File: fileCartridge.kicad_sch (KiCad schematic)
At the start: 20 parts, among them U11 74AHCV17A, U12 74LVC3G17, U13 SN74LVC8T245, U14 SN74LVC8T245, U5 74LVC06A, U8 74LVC1G06, U9 SN74LVC8T245

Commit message: Fix some checker complaints
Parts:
- CART1: value (none) -> CARTRIDGE_C64; footprint (none) -> icomp:CARTRIDGE_C64_GERMAN
- X1: value (none) -> EXPANSION_PORT_C64_EDGE; footprint (none) -> RETRO_Innovations:MA100-22-2
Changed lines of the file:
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@@
     (comment 4 "Based on Orange Crab by Gregory Davill")
   )
+  (bus_alias "A_HIGH" (members "8" "9" "10" "11" "12" "13" "14" "15"))
   (junction (at 115.57 34.29) (diameter 0) (color 0 0 0 0)
   )
@@
     (stroke (width 0) (type default) (color 0 0 0 0))
   )
-  (wire (pts (xy 41.91 87.63) (xy 35.56 87.63))
+  (wire (pts (xy 41.91 87.63) (xy 39.37 87.63))
     (stroke (width 0) (type default) (color 0 0 0 0))
   )
@@
     (stroke (width 0) (type default) (color 0 0 0 0))
   )
-  (wire (pts (xy 24.13 91.44) (xy 19.05 91.44))
+  (wire (pts (xy 24.13 91.44) (xy 22.86 91.44))
     (stroke (width 0) (type default) (color 0 0 0 0))
   )
@@
     (effects (font (size 1.27 1.27)) (justify right bottom))
   )
-  (label "VCC" (at 203.2 92.71 180)
-    (effects (font (size 1.27 1.27)) (justify right bottom))
-  )
   (label "CINT6" (at 226.06 142.24 0)
     (effects (font (size 1.27 1.27)) (justify left bottom))
@@
     (effects (font (size 1.27 1.27)) (justify left bottom))
   )
-  (label "VCC" (at 35.56 87.63 0)
-    (effects (font (size 1.27 1.27)) (justify left bottom))
+  (label "{A_HIGH}" (at 171.45 92.71 180)
+    (effects (font (size 1.27 1.27)) (justify right bottom))
   )
   (label "10" (at 121.92 87.63 180)
@@
     (effects (font (size 1.27 1.27)) (justify left bottom))
   )
-  (label "VCC" (at 151.13 92.71 180)
-    (effects (font (size 1.27 1.27)) (justify right bottom))
-  )
   (label "15" (at 176.53 80.01 0)
     (effects (font (size 1.27 1.27)) (justify left bottom))
@@
   )
   (label "CD23" (at 74.93 74.93 0)
-    (effects (font (size 1.27 1.27)) (justify left bottom))
-  )
-  (label "VCC" (at 19.05 91.44 0)
     (effects (font (size 1.27 1.27)) (justify left bottom))
   )
@@
     )
   )
+  (global_label "P3.3V" (shape passive) (at 203.2 92.71 0) (fields_autoplaced)
+    (effects (font (size 1.27 1.27)) (justify left))
+    (property "Intersheet References" "${INTERSHEET_REFS}" (id 0) (at -62.23 -35.56 0)
+      (effects (font (size 1.27 1.27)) hide)
+    )
+  )
   (global_label "GAME" (shape input) (at 27.94 175.26 270) (fields_autoplaced)
     (effects (font (size 1.27 1.27)) (justify right))
@@
     )
   )
+  (global_label "P3.3V" (shape passive) (at 22.86 91.44 180) (fields_autoplaced)
+    (effects (font (size 1.27 1.27)) (justify right))
+    (property "Intersheet References" "${INTERSHEET_REFS}" (id 0) (at 288.29 219.71 0)
+      (effects (font (size 1.27 1.27)) hide)
+    )
+  )
   (global_label "EXROM" (shape input) (at 39.37 175.26 270) (fields_autoplaced)
     (effects (font (size 1.27 1.27)) (justify right))
@@
     )
   )
+  (global_label "P3.3V" (shape passive) (at 39.37 87.63 180) (fields_autoplaced)
+    (effects (font (size 1.27 1.27)) (justify right))
+    (property "Intersheet References" "${INTERSHEET_REFS}" (id 0) (at 304.8 215.9 0)
+      (effects (font (size 1.27 1.27)) hide)
+    )
+  )
   (global_label "A12" (shape bidirectional) (at 213.36 72.39 0) (fields_autoplaced)
     (effects (font (size 1.27 1.27)) (justify left))
@@
     )
   )
+  (global_label "P3.3V" (shape passive) (at 151.13 92.71 0) (fields_autoplaced)
+    (effects (font (size 1.27 1.27)) (justify left))
+    (property "Intersheet References" "${INTERSHEET_REFS}" (id 0) (at -114.3 -35.56 0)
+      (effects (font (size 1.27 1.27)) hide)
+    )
+  )
   (global_label "D_DIR" (shape input) (at 25.4 80.01 180) (fields_autoplaced)
     (effects (font (size 1.27 1.27)) (justify right))
@@
     )
   )
-  (symbol (lib_id "RETRO_Innovations:EXPANSION_PORT_C64_EDGE") (at 96.52 87.63 0) (mirror y) (unit 1)
+  (symbol (lib_name "EXPANSION_PORT_C64_EDGE_1") (lib_id "RETRO_Innovations:EXPANSION_PORT_C64_EDGE") (at 96.52 87.63 0) (mirror y) (unit 1)
     (in_bom no) (on_board yes)
     (property "Reference" "X1" (id 0) (at 96.52 52.578 0)
       (effects (font (size 1.4986 1.4986)))
     )
-    (property "Value" "" (id 1) (at 106.68 133.35 0)
+    (property "Value" "EXPANSION_PORT_C64_EDGE" (id 1) (at 86.36 133.35 0)
       (effects (font (size 1.4986 1.4986)) (justify left bottom) hide)
     )
-    (property "Footprint" "" (id 2) (at 96.52 87.63 0)
+    (property "Footprint" "RETRO_Innovations:MA100-22-2" (id 2) (at 96.52 87.63 0)
       (effects (font (size 1.27 1.27)) hide)
     )
@@
       (effects (font (size 1.4986 1.4986)) (justify left))
     )
-    (property "Value" "" (id 1) (at 241.3 113.03 0)
+    (property "Value" "EXPANSION_PORT_C64_EDGE" (id 1) (at 241.3 113.03 0)
       (effects (font (size 1.4986 1.4986)) (justify left bottom) hide)
     )
-    (property "Footprint" "" (id 2) (at 251.46 67.31 0)
+    (property "Footprint" "RETRO_Innovations:MA100-22-2" (id 2) (at 251.46 67.31 0)
       (effects (font (size 1.27 1.27)) hide)
     )
@@
       (effects (font (size 1.4986 1.4986)) (justify left))
     )
-    (property "Value" "" (id 1) (at 254 34.29 0)
-      (effects (font (size 1.27 1.27)) hide)
-    )
-    (property "Footprint" "" (id 2) (at 254 34.29 0)
-      (effects (font (size 1.27 1.27)) hide)
-    )
+    (property "Value" "CARTRIDGE_C64" (id 1) (at 254 34.29 0)
+      (effects (font (size 1.27 1.27)) hide)
+    )
+    (property "Footprint" "icomp:CARTRIDGE_C64_GERMAN" (id 2) (at 254 34.29 0)
+      (effects (font (size 1.27 1.27)) hide)
+    )

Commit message: Update Mouser prices
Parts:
- C4: Pricing (EUR) 0,04 -> 0,10
- U11: Pricing (EUR) 0,42 -> 0,44
- U12: Pricing (EUR) 0.47 -> 0.66
- U13, U14, U9: Pricing (EUR) 1,44 -> 1,56
- U5: Pricing (EUR) 0.35 -> 1,01
- U8: Pricing (EUR) 0.27 -> 0.34
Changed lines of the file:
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@@
       (effects (font (size 1.27 1.27)) hide)
     )
-    (property "Pricing (EUR)" "1,44" (id 5) (at 44.45 69.85 0)
+    (property "Pricing (EUR)" "1,56" (id 5) (at 44.45 69.85 0)
       (effects (font (size 1.27 1.27)) hide)
     )
@@
       (effects (font (size 1.27 1.27)) hide)
     )
-    (property "Pricing (EUR)" "1,44" (id 5) (at 194.31 74.93 0)
+    (property "Pricing (EUR)" "1,56" (id 5) (at 194.31 74.93 0)
       (effects (font (size 1.27 1.27)) hide)
     )
@@
       (effects (font (size 1.27 1.27)) hide)
     )
-    (property "Pricing (EUR)" "1,44" (id 5) (at 142.24 74.93 0)
+    (property "Pricing (EUR)" "1,56" (id 5) (at 142.24 74.93 0)
       (effects (font (size 1.27 1.27)) hide)
     )
@@
       (effects (font (size 1.27 1.27)) hide)
     )
-    (property "Pricing (EUR)" "0.27" (id 5) (at 49.53 152.4 0)
+    (property "Pricing (EUR)" "0.34" (id 5) (at 49.53 152.4 0)
       (effects (font (size 1.27 1.27)) hide)
     )
@@
       (effects (font (size 1.27 1.27)) hide)
     )
-    (property "Pricing (EUR)" "0,42" (id 5) (at 173.99 125.73 0)
+    (property "Pricing (EUR)" "0,44" (id 5) (at 173.99 125.73 0)
       (effects (font (size 1.27 1.27)) hide)
     )
@@
       (effects (font (size 1.27 1.27)) hide)
     )
-    (property "Pricing (EUR)" "0,42" (id 5) (at 114.3 143.51 0)
+    (property "Pricing (EUR)" "0,44" (id 5) (at 114.3 143.51 0)
       (effects (font (size 1.27 1.27)) hide)
     )
@@
       (effects (font (size 1.27 1.27)) hide)
     )
-    (property "Pricing (EUR)" "0,42" (id 5) (at 128.27 34.29 0)
+    (property "Pricing (EUR)" "0,44" (id 5) (at 128.27 34.29 0)
       (effects (font (size 1.27 1.27)) hide)
     )
@@
       (effects (font (size 1.27 1.27)) hide)
     )
-    (property "Pricing (EUR)" "0,42" (id 5) (at 173.99 105.41 0)
+    (property "Pricing (EUR)" "0,44" (id 5) (at 173.99 105.41 0)
       (effects (font (size 1.27 1.27)) hide)
     )
@@
       (effects (font (size 1.27 1.27)) hide)
     )
-    (property "Pricing (EUR)" "0,42" (id 5) (at 165.1 114.3 0)
+    (property "Pricing (EUR)" "0,44" (id 5) (at 165.1 114.3 0)
       (effects (font (size 1.27 1.27)) hide)
     )
@@
       (effects (font (size 1.27 1.27)) hide)
     )
-    (property "Pricing (EUR)" "0.35" (id 5) (at 39.37 142.24 0)
+    (property "Pricing (EUR)" "1,01" (id 5) (at 39.37 142.24 0)
       (effects (font (size 1.27 1.27)) hide)
     )
@@
       (effects (font (size 1.27 1.27)) hide)
     )
-    (property "Pricing (EUR)" "0.35" (id 5) (at 27.94 152.4 0)
+    (property "Pricing (EUR)" "1,01" (id 5) (at 27.94 152.4 0)
       (effects (font (size 1.27 1.27)) hide)
     )
@@
       (effects (font (size 1.27 1.27)) hide)
     )
-    (property "Pricing (EUR)" "0.35" (id 5) (at 166.37 134.62 0)
+    (property "Pricing (EUR)" "1,01" (id 5) (at 166.37 134.62 0)
       (effects (font (size 1.27 1.27)) hide)
     )
@@
       (effects (font (size 1.27 1.27)) hide)
     )
-    (property "Pricing (EUR)" "0.35" (id 5) (at 80.01 142.24 0)
+    (property "Pricing (EUR)" "1,01" (id 5) (at 80.01 142.24 0)
       (effects (font (size 1.27 1.27)) hide)
     )
@@
       (effects (font (size 1.27 1.27)) hide)
     )
-    (property "Pricing (EUR)" "0.35" (id 5) (at 69.85 151.13 0)
+    (property "Pricing (EUR)" "1,01" (id 5) (at 69.85 151.13 0)
       (effects (font (size 1.27 1.27)) hide)
     )
@@
       (effects (font (size 1.27 1.27)) hide)
     )
-    (property "Pricing (EUR)" "0.35" (id 5) (at 105.41 34.29 0)
+    (property "Pricing (EUR)" "1,01" (id 5) (at 105.41 34.29 0)
       (effects (font (size 1.27 1.27)) hide)
     )
@@
       (effects (font (size 1.27 1.27)) hide)
     )
-    (property "Pricing (EUR)" "0,04" (id 5) (at 251.46 104.14 0)
+    (property "Pricing (EUR)" "0,10" (id 5) (at 251.46 104.14 0)
       (effects (font (size 1.27 1.27)) hide)
     )
@@
       (effects (font (size 1.27 1.27)) hide)
     )
-    (property "Pricing (EUR)" "0,42" (id 7) (at 140.97 153.67 0)
+    (property "Pricing (EUR)" "0,44" (id 7) (at 140.97 153.67 0)
       (effects (font (size 1.27 1.27)) hide)
     )
@@
       (effects (font (size 1.27 1.27)) hide)
     )
-    (property "Pricing (EUR)" "0.47" (id 5) (at 123.19 153.67 0)
+    (property "Pricing (EUR)" "0.66" (id 5) (at 123.19 153.67 0)
       (effects (font (size 1.27 1.27)) hide)
     )
@@
       (effects (font (size 1.27 1.27)) hide)
     )
-    (property "Pricing (EUR)" "0.47" (id 5) (at 60.96 143.51 0)
+    (property "Pricing (EUR)" "0.66" (id 5) (at 60.96 143.51 0)
       (effects (font (size 1.27 1.27)) hide)
     )
@@
       (effects (font (size 1.27 1.27)) hide)
     )
-    (property "Pricing (EUR)" "0.47" (id 5) (at 132.08 143.51 0)
-      (effects (font (size 1.27 1.27)) hide)
-    )
+    (property "Pricing (EUR)" "0.66" (id 5) (at 132.08 143.51 0)
+      (effects (font (size 1.27 1.27)) hide)
+    )

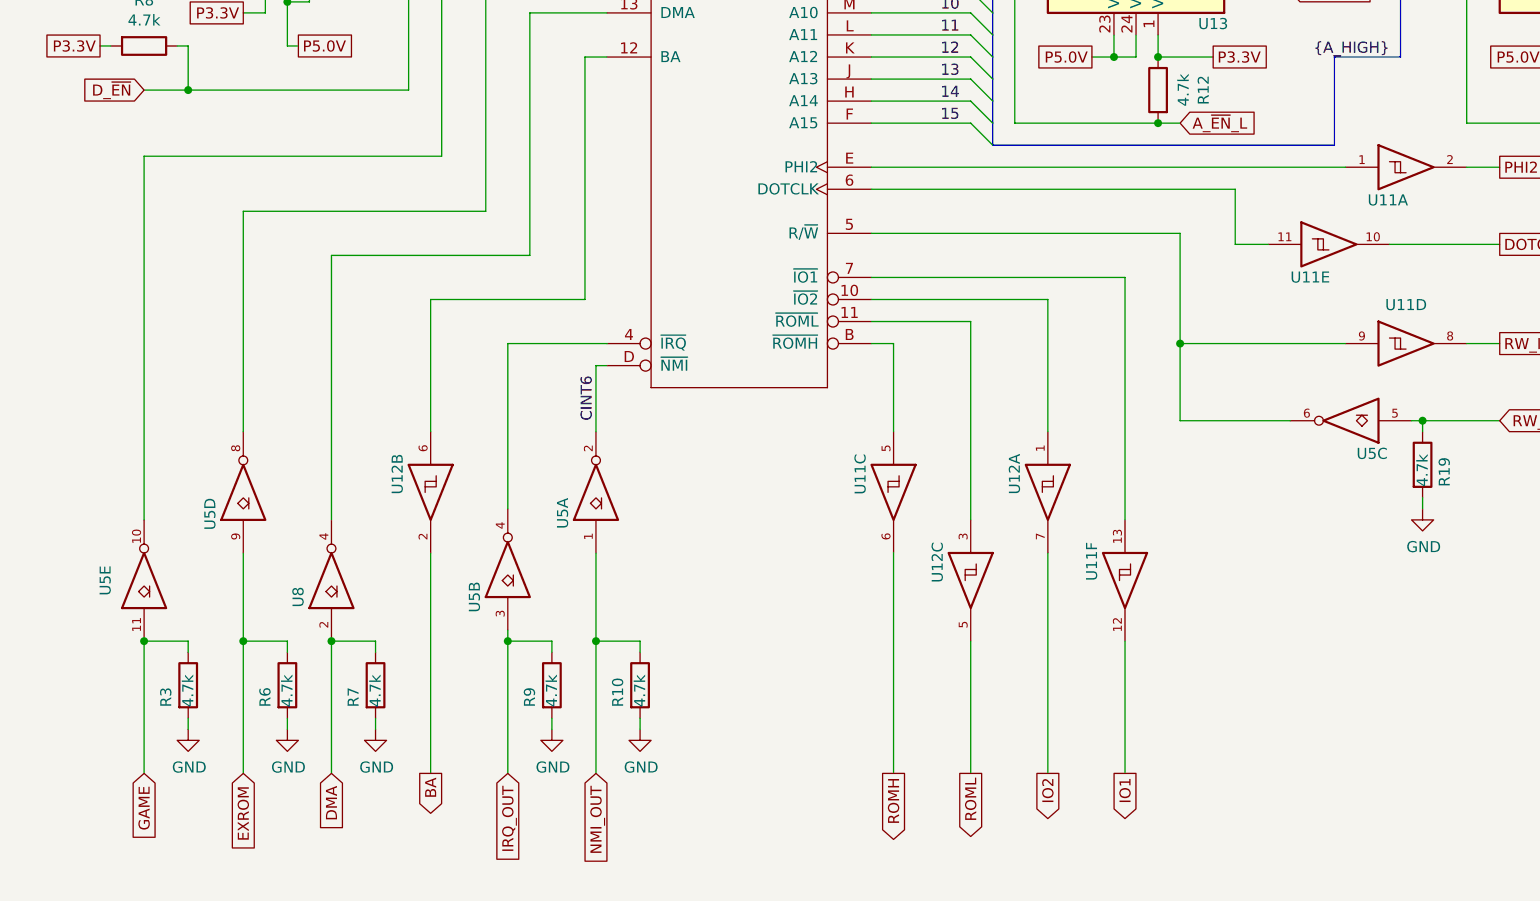
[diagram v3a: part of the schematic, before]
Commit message: Add NMI and IRQ inputs
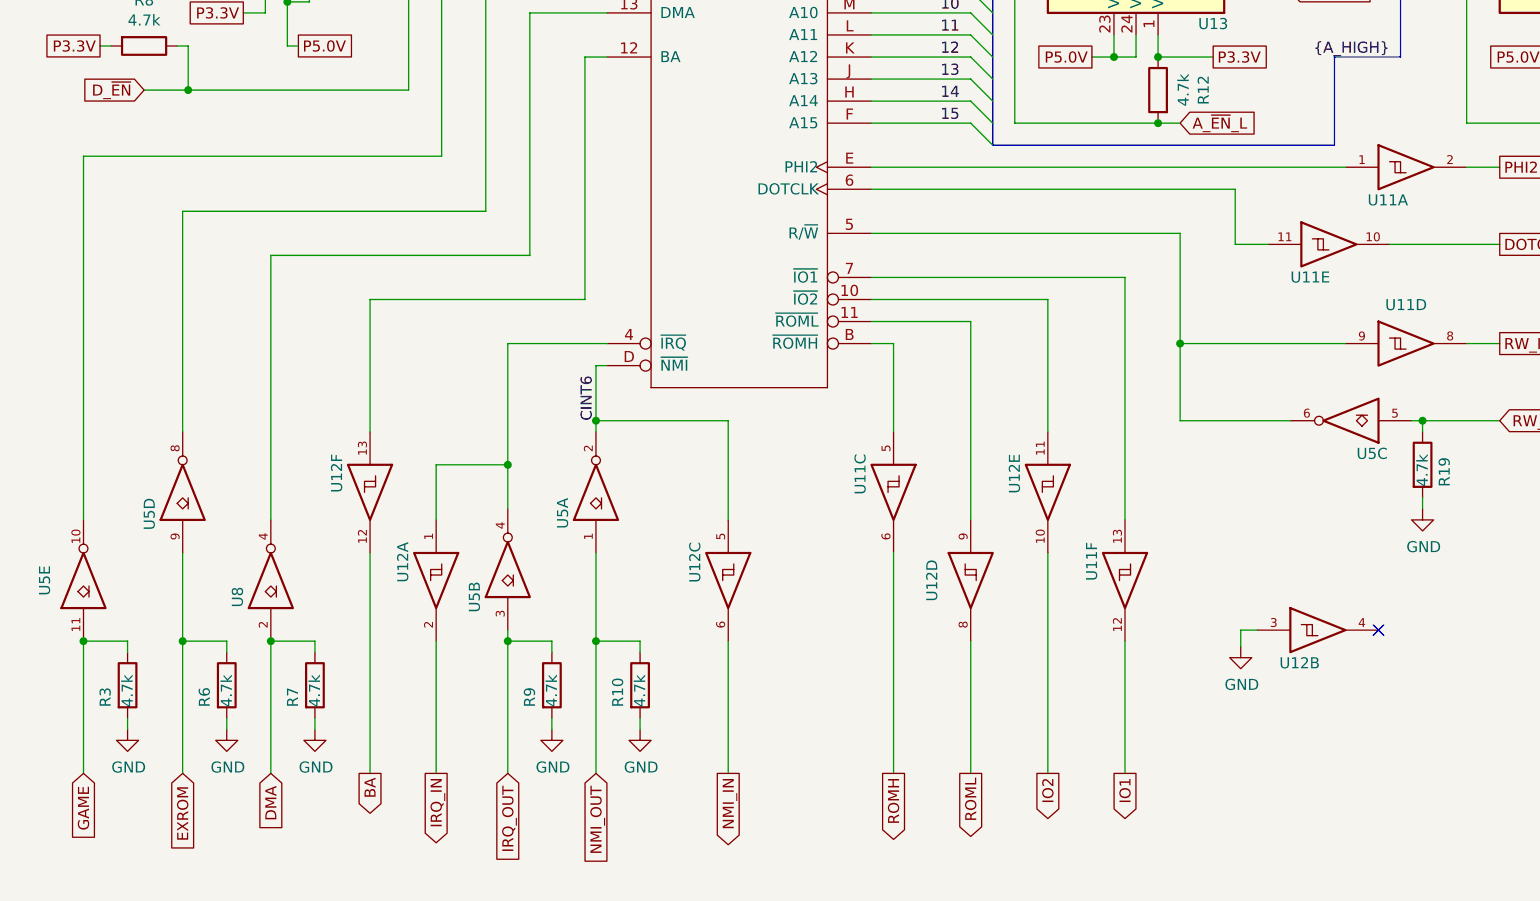
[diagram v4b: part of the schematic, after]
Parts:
- removed U12: 74LVC3G17, Package_SO:TSSOP-8_3x3mm_P0.65mm, symbol 74xGxx:74LVC3G17
- added U12: 74AHCV17A, Package_SO:TSSOP-14_4.4x5mm_P0.65mm, symbol buffers:74AHCV17A
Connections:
- net BA: now also U12.12
- net CINT6: now also U12.5
- net GND: now also U12.3, U12.7 (GND), U12.7 (GND), U12.7 (GND), U12.7 (GND), U12.7 (GND), U12.7 (GND)
- net IO2: now also U12.10
- net ROML: now also U12.8
- net VCC: now also U12.14 (VCC), U12.14 (VCC), U12.14 (VCC), U12.14 (VCC), U12.14 (VCC), U12.14 (VCC)
- net at X1.10 (~{IO2}): now also U12.11
- net at X1.11 (~{ROML}): now also U12.9
- net at X1.12 (BA): now also U12.13
- net at U5.4, X1.4 (~{IRQ}): now also U12.1
- new net IRQ_IN: U12.2
- new net NMI_IN: U12.6
- no-connect marks 0 -> 1
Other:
- moved on the sheet: R3, R6, R7, U5D, U5E, U8

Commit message: Replace 8-channel level shifters with LVCH variant
The "H" makes them consume less current when the inputs are floating.
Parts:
- U13, U14, U9: value SN74LVC8T245 -> 74LVCH8T245; Mfg TI -> Nexperia; Mouser Part No 595-SN74LVC8T245PWR -> 771-4LVCH8T245PWQ10J; PN SN74LVC8T245PWR -> 74LVCH8T245PW-Q10J; Pricing (EUR) 1,56 -> 1,35
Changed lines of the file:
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@@
     (in_bom yes) (on_board yes)
     (property "Reference" "U9" (id 0) (at 35.56 53.34 0))
-    (property "Value" "SN74LVC8T245" (id 1) (at 44.45 68.58 90)
+    (property "Value" "74LVCH8T245" (id 1) (at 44.45 68.58 90)
       (effects (font (size 0.9906 0.9906)))
     )
@@
       (effects (font (size 1.27 1.27)) hide)
     )
-    (property "Datasheet" "http://www.ti.com/lit/ds/symlink/sn74lvc8t245.pdf" (id 3) (at 43.18 63.5 0)
+    (property "Datasheet" "https://assets.nexperia.com/documents/data-sheet/74LVC_LVCH8T245.pdf" (id 3) (at 43.18 63.5 0)
       (effects (font (size 1.27 1.27)) hide)
     )
-    (property "Mouser Part No" "595-SN74LVC8T245PWR" (id 4) (at 44.45 69.85 0)
+    (property "Mouser Part No" "771-4LVCH8T245PWQ10J" (id 4) (at 44.45 69.85 0)
       (effects (font (size 1.27 1.27)) hide)
     )
-    (property "Pricing (EUR)" "1,56" (id 5) (at 44.45 69.85 0)
+    (property "Pricing (EUR)" "1,35" (id 5) (at 44.45 69.85 0)
       (effects (font (size 1.27 1.27)) hide)
     )
-    (property "Mfg" "TI" (id 6) (at 44.45 69.85 0)
+    (property "Mfg" "Nexperia" (id 6) (at 44.45 69.85 0)
       (effects (font (size 1.27 1.27)) hide)
     )
-    (property "PN" "SN74LVC8T245PWR" (id 7) (at 44.45 69.85 0)
+    (property "PN" "74LVCH8T245PW-Q10J" (id 7) (at 44.45 69.85 0)
       (effects (font (size 1.27 1.27)) hide)
     )
@@
     (in_bom yes) (on_board yes)
     (property "Reference" "U14" (id 0) (at 203.2 88.9 0))
-    (property "Value" "SN74LVC8T245" (id 1) (at 194.31 72.39 90)
+    (property "Value" "74LVCH8T245" (id 1) (at 194.31 72.39 90)
       (effects (font (size 0.9906 0.9906)))
     )
@@
       (effects (font (size 1.27 1.27)) hide)
     )
-    (property "Datasheet" "http://www.ti.com/lit/ds/symlink/sn74lvc8t245.pdf" (id 3) (at 195.58 68.58 0)
+    (property "Datasheet" "https://assets.nexperia.com/documents/data-sheet/74LVC_LVCH8T245.pdf" (id 3) (at 195.58 68.58 0)
       (effects (font (size 1.27 1.27)) hide)
     )
-    (property "Mouser Part No" "595-SN74LVC8T245PWR" (id 4) (at 194.31 74.93 0)
+    (property "Mouser Part No" "771-4LVCH8T245PWQ10J" (id 4) (at 194.31 74.93 0)
       (effects (font (size 1.27 1.27)) hide)
     )
-    (property "Pricing (EUR)" "1,56" (id 5) (at 194.31 74.93 0)
+    (property "Pricing (EUR)" "1,35" (id 5) (at 194.31 74.93 0)
       (effects (font (size 1.27 1.27)) hide)
     )
-    (property "Mfg" "TI" (id 6) (at 194.31 74.93 0)
+    (property "Mfg" "Nexperia" (id 6) (at 194.31 74.93 0)
       (effects (font (size 1.27 1.27)) hide)
     )
-    (property "PN" "SN74LVC8T245PWR" (id 7) (at 194.31 74.93 0)
+    (property "PN" "74LVCH8T245PW-Q10J" (id 7) (at 194.31 74.93 0)
       (effects (font (size 1.27 1.27)) hide)
     )
@@
     (in_bom yes) (on_board yes)
     (property "Reference" "U13" (id 0) (at 151.13 88.9 0))
-    (property "Value" "SN74LVC8T245" (id 1) (at 142.24 72.39 90)
+    (property "Value" "74LVCH8T245" (id 1) (at 142.24 72.39 90)
       (effects (font (size 0.9906 0.9906)))
     )
@@
       (effects (font (size 1.27 1.27)) hide)
     )
-    (property "Datasheet" "http://www.ti.com/lit/ds/symlink/sn74lvc8t245.pdf" (id 3) (at 143.51 68.58 0)
+    (property "Datasheet" "https://assets.nexperia.com/documents/data-sheet/74LVC_LVCH8T245.pdf" (id 3) (at 143.51 68.58 0)
       (effects (font (size 1.27 1.27)) hide)
     )
-    (property "Mouser Part No" "595-SN74LVC8T245PWR" (id 4) (at 142.24 74.93 0)
+    (property "Mouser Part No" "771-4LVCH8T245PWQ10J" (id 4) (at 142.24 74.93 0)
       (effects (font (size 1.27 1.27)) hide)
     )
-    (property "Pricing (EUR)" "1,56" (id 5) (at 142.24 74.93 0)
+    (property "Pricing (EUR)" "1,35" (id 5) (at 142.24 74.93 0)
       (effects (font (size 1.27 1.27)) hide)
     )
-    (property "Mfg" "TI" (id 6) (at 142.24 74.93 0)
+    (property "Mfg" "Nexperia" (id 6) (at 142.24 74.93 0)
       (effects (font (size 1.27 1.27)) hide)
     )
-    (property "PN" "SN74LVC8T245PWR" (id 7) (at 142.24 74.93 0)
+    (property "PN" "74LVCH8T245PW-Q10J" (id 7) (at 142.24 74.93 0)
       (effects (font (size 1.27 1.27)) hide)
     )
